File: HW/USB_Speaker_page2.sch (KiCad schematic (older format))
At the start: 3 parts

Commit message: Amplifier circuit using TPA6211A1-Q1
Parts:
- removed U?: OPA1678, symbol OPA1678
- added C14, C16: 10uF, symbol C_Small
- added C15, C17: 0.1uF, symbol C_Small
- added C? (x2): 0.22uF, symbol C_Small
- added U2, U3: TPA6211A1-Q1, symbol TPA6211A1-Q1
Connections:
- net labels added: GND, VBUS
- wire segments 0 -> 42
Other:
- moved on the sheet: LS1, LS2

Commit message: Switching out 2x TPA6211A1 for 1x TPA3137D2
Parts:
- added C? (x2): 1nF, symbol C_Small
- added C? (x2): 100nF, symbol C_Small
- added C? (x2): 10uF, symbol CP1_Small
- added C? (x2): 1uF, symbol C_Small
- added R? (x3): 10K, symbol R
- added U?: TPA3137D2, symbol TPA3137D2
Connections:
- wire segments 42 -> 98
- no-connect marks 0 -> 3
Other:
- note added: "PVCCL"
- note added: "PVCCR"

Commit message: Finsihed drawing amp circuit. Adding options and values later
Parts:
- removed C14, C16: 10uF, symbol C_Small
- removed C15, C17: 0.1uF, symbol C_Small
- removed C? (x2): 0.22uF, symbol C_Small
- removed R? (x2): 10K, symbol R
- removed U2, U3: TPA6211A1-Q1, symbol TPA6211A1-Q1
- added C? (x8): 1uF, symbol C_Small
- added C? (x4): 0.22uF, symbol C_Small
- added L? (x4): ?, symbol Ferrite_Bead_Small
- added R?: 10, symbol R
- added R?: NP, symbol R
- added R?: 0.0, symbol R
- added R? (x2): ?, symbol R
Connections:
- net labels added: PBTL, PLIMIT, Vin_L, Vin_R
- wire segments 98 -> 100
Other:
- note removed: "PVCCL"
- note removed: "PVCCR"
- moved on the sheet: C?, LS1, LS2, R?, U?

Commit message: ferrite chosen
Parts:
- L? (x4): value ? -> 300Ω@100MHz
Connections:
- net at R?.2, U?.1 (SDn): no longer U?.2 (FAULTn)
- new net FAULT: U?.2 (FAULTn)
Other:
- note added: "AND Gate \nhere"
- note added: "Use NFZ2MSM as output filter ferrite bead"
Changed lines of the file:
@@
 Connection ~ 5200 2700
 Wire Wire Line
-	3400 2050 3400 2500
-Wire Wire Line
 	3400 1750 3400 1650
 Wire Wire Line
-	3400 2300 3600 2300
-Wire Wire Line
-	3400 2500 3600 2500
+	2700 2300 3600 2300
+Wire Wire Line
+	3300 2500 3600 2500
 Connection ~ 3400 2300
 Wire Wire Line
@@
 Wire Wire Line
 	6200 3200 6200 3100
-Wire Wire Line
-	5800 3100 6400 3100
 Wire Wire Line
 	6400 3100 6400 3400
@@
 P 5700 3800
 F 0 "L?" V 5650 3700 50  0000 L CNN
-F 1 "?" V 5650 3900 50  0000 L CNN
+F 1 "300Ω@100MHz" V 5800 3650 50  0000 L CNN
 F 2 "" V 5630 3800 50  0001 C CNN
 F 3 "" H 5700 3800 50  0001 C CNN
@@
 P 5700 3100
 F 0 "L?" V 5650 3000 50  0000 L CNN
-F 1 "?" V 5650 3200 50  0000 L CNN
+F 1 "300Ω@100MHz" V 5800 2950 50  0000 L CNN
 F 2 "" V 5630 3100 50  0001 C CNN
 F 3 "" H 5700 3100 50  0001 C CNN
@@
 $EndComp
 Connection ~ 5150 3100
-Wire Wire Line
-	6000 3100 6000 3100
 Connection ~ 6200 3100
 Connection ~ 5150 3800
@@
 P 5700 4800
 F 0 "L?" V 5650 4700 50  0000 L CNN
-F 1 "?" V 5650 4900 50  0000 L CNN
+F 1 "300Ω@100MHz" V 5850 4650 50  0000 L CNN
 F 2 "" V 5630 4800 50  0001 C CNN
 F 3 "" H 5700 4800 50  0001 C CNN
@@
 P 5700 4100
 F 0 "L?" V 5650 4000 50  0000 L CNN
-F 1 "?" V 5650 4200 50  0000 L CNN
+F 1 "300Ω@100MHz" V 5800 3950 50  0000 L CNN
 F 2 "" V 5630 4100 50  0001 C CNN
 F 3 "" H 5700 4100 50  0001 C CNN
@@
 	3600 4500 2900 4500
 Connection ~ 2900 4500
+Text HLabel 1550 1900 0    60   Input ~ 0
+SSPNDn
+Wire Wire Line
+	3400 2050 3400 2300
+Text Label 3300 2500 0    60   ~ 0
+FAULT
+Text Label 1200 2100 0    60   ~ 0
+FAULT
+Wire Wire Line
+	1550 1900 1750 1900
+Wire Wire Line
+	1200 2100 1750 2100
+Wire Notes Line
+	1750 2200 1750 1750
+Wire Notes Line
+	1750 1750 2300 1750
+Wire Notes Line
+	2300 1750 2300 2200
+Wire Notes Line
+	2300 2200 1750 2200
+Wire Wire Line
+	2300 2000 2700 2000
+Wire Wire Line
+	2700 2000 2700 2300
+Text Notes 1850 2050 0    60   ~ 0
+AND Gate \nhere
+Wire Wire Line
+	5800 3100 6400 3100
+Text Notes 5600 2950 0    60   ~ 0
+Use NFZ2MSM as output filter ferrite bead
 $EndSCHEMATC

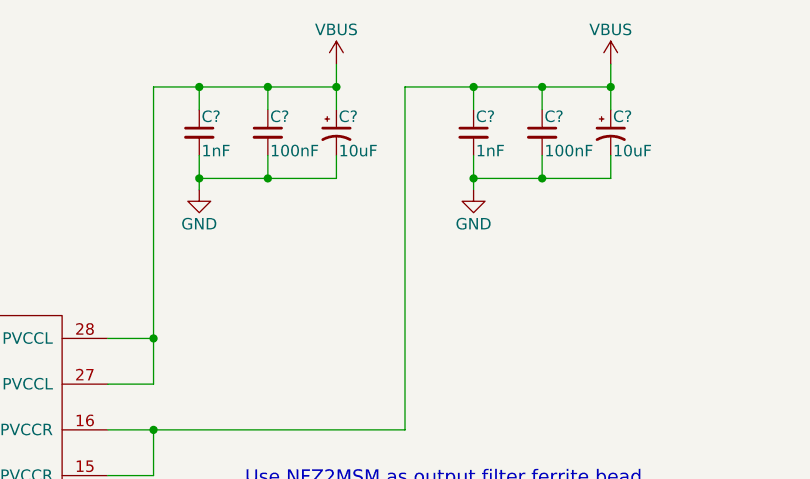
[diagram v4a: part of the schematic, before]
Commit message: Basic battery power supply topology
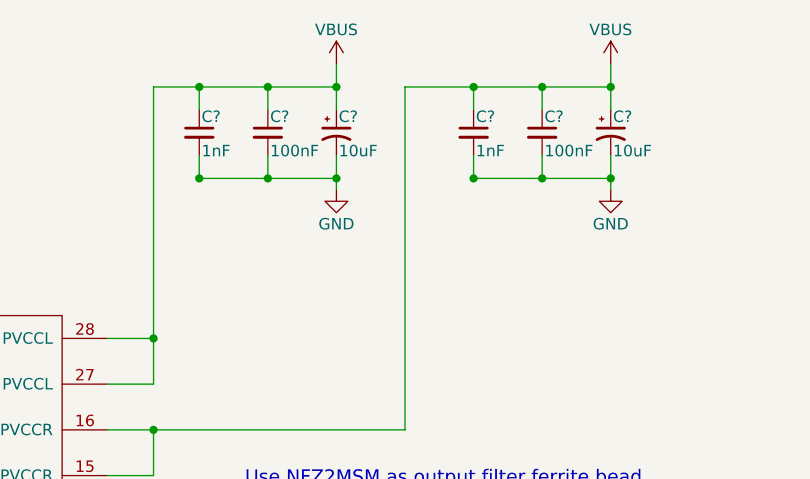
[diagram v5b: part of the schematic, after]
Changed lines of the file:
@@
 $Descr A4 11693 8268
 encoding utf-8
-Sheet 2 2
+Sheet 2 3
 Title ""
 Date ""
@@
 $EndComp
 $Comp
-L GND #PWR?
-U 1 1 5B29E616
-P 5400 1650
-F 0 "#PWR?" H 5400 1400 50  0001 C CNN
-F 1 "GND" H 5400 1500 50  0000 C CNN
-F 2 "" H 5400 1650 50  0001 C CNN
-F 3 "" H 5400 1650 50  0001 C CNN
-	1    5400 1650
-	1    0    0    -1
-$EndComp
-$Comp
 L C_Small C?
 U 1 1 5B2A1B92
@@
 L GND #PWR?
 U 1 1 5B2A1BAA
-P 6600 1650
-F 0 "#PWR?" H 6600 1400 50  0001 C CNN
-F 1 "GND" H 6600 1500 50  0000 C CNN
-F 2 "" H 6600 1650 50  0001 C CNN
-F 3 "" H 6600 1650 50  0001 C CNN
-	1    6600 1650
+P 7200 1650
+F 0 "#PWR?" H 7200 1400 50  0001 C CNN
+F 1 "GND" H 7200 1500 50  0000 C CNN
+F 2 "" H 7200 1650 50  0001 C CNN
+F 3 "" H 7200 1650 50  0001 C CNN
+	1    7200 1650
 	1    0    0    -1
 $EndComp
@@
 	6000 1100 6000 1300
 Wire Wire Line
-	5400 1500 5400 1650
+	5400 1500 5400 1600
 Connection ~ 6000 1200
 Wire Wire Line
@@
 	5400 1600 6000 1600
 Wire Wire Line
-	6000 1600 6000 1500
+	6000 1500 6000 1650
 Connection ~ 5700 1600
 Connection ~ 5400 1600
@@
 	6300 1200 7200 1200
 Wire Wire Line
-	6600 1500 6600 1650
+	6600 1500 6600 1600
 Connection ~ 7200 1200
 Wire Wire Line
@@
 	6600 1600 7200 1600
 Wire Wire Line
-	7200 1600 7200 1500
+	7200 1500 7200 1650
 Connection ~ 6900 1600
 Connection ~ 6600 1600
@@
 Text Notes 5600 2950 0    60   ~ 0
 Use NFZ2MSM as output filter ferrite bead
+$Comp
+L GND #PWR?
+U 1 1 5B29E616
+P 6000 1650
+F 0 "#PWR?" H 6000 1400 50  0001 C CNN
+F 1 "GND" H 6000 1500 50  0000 C CNN
+F 2 "" H 6000 1650 50  0001 C CNN
+F 3 "" H 6000 1650 50  0001 C CNN
+	1    6000 1650
+	1    0    0    -1
+$EndComp
+Connection ~ 6000 1600
+Connection ~ 7200 1600
 $EndSCHEMATC

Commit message: What did I do?
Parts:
- added C?: 1uF, symbol C_Small
- added U?: BU4S81G2, symbol BU4S81G2
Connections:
- net GND: now also C?.2, U?.3 (GND)
- net SSPNDn: now also U?.1 (A)
- net at R?.2, U?.1 (SDn): now also U?.4 (Y)
- net FAULT renamed FAULTn
- net FAULTn: now also U?.2 (B)
- net VBUS renamed +BATT
- net +BATT: now also C?.1, U?.5 (VCC)
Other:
- note added: "If SSDPNDn or FAULTn are active (LOW), shutdown ampifier"
- note removed: "AND Gate \nhere"
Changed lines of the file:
@@
-$EndComp
-$Comp
-L VBUS #PWR?
-U 1 1 5B29E207
-P 6000 1100
-F 0 "#PWR?" H 6000 950 50  0001 C CNN
-F 1 "VBUS" H 6000 1250 50  0000 C CNN
-F 2 "" H 6000 1100 50  0001 C CNN
-F 3 "" H 6000 1100 50  0001 C CNN
-	1    6000 1100
-	1    0    0    -1
 $EndComp
 $Comp
@@
 $EndComp
 $Comp
-L VBUS #PWR?
-U 1 1 5B2A1BA4
-P 7200 1100
-F 0 "#PWR?" H 7200 950 50  0001 C CNN
-F 1 "VBUS" H 7200 1250 50  0000 C CNN
-F 2 "" H 7200 1100 50  0001 C CNN
-F 3 "" H 7200 1100 50  0001 C CNN
-	1    7200 1100
-	1    0    0    -1
-$EndComp
-$Comp
 L GND #PWR?
 U 1 1 5B2A1BAA
@@
 F 3 "" H 7200 1650 50  0001 C CNN
 	1    7200 1650
-	1    0    0    -1
-$EndComp
-$Comp
-L VBUS #PWR?
-U 1 1 5B2A2F62
-P 3400 1650
-F 0 "#PWR?" H 3400 1500 50  0001 C CNN
-F 1 "VBUS" H 3400 1800 50  0000 C CNN
-F 2 "" H 3400 1650 50  0001 C CNN
-F 3 "" H 3400 1650 50  0001 C CNN
-	1    3400 1650
 	1    0    0    -1
 $EndComp
@@
 $EndComp
 $Comp
-L VBUS #PWR?
-U 1 1 5B2B0A32
-P 1450 3650
-F 0 "#PWR?" H 1450 3500 50  0001 C CNN
-F 1 "VBUS" H 1450 3800 50  0000 C CNN
-F 2 "" H 1450 3650 50  0001 C CNN
-F 3 "" H 1450 3650 50  0001 C CNN
-	1    1450 3650
-	1    0    0    -1
-$EndComp
-$Comp
 L R R?
 U 1 1 5B2B163A
@@
 $EndComp
 $Comp
-L VBUS #PWR?
-U 1 1 5B2B27B1
-P 2900 4000
-F 0 "#PWR?" H 2900 3850 50  0001 C CNN
-F 1 "VBUS" H 2900 4150 50  0000 C CNN
-F 2 "" H 2900 4000 50  0001 C CNN
-F 3 "" H 2900 4000 50  0001 C CNN
-	1    2900 4000
-	1    0    0    -1
-$EndComp
-$Comp
 L TPA3137D2 U?
 U 1 1 5B29D076
 P 3800 5400
-F 0 "U?" H 3850 8550 60  0000 C CNN
+F 0 "U?" H 3850 8650 60  0000 C CNN
 F 1 "TPA3137D2" H 4050 5450 60  0000 C CNN
 F 2 "" H 3800 5550 60  0001 C CNN
@@
 $EndComp
 $Comp
-L VBUS #PWR?
-U 1 1 5B2B5C0D
-P 1200 3650
-F 0 "#PWR?" H 1200 3500 50  0001 C CNN
-F 1 "VBUS" H 1200 3800 50  0000 C CNN
-F 2 "" H 1200 3650 50  0001 C CNN
-F 3 "" H 1200 3650 50  0001 C CNN
-	1    1200 3650
-	1    0    0    -1
-$EndComp
-$Comp
 L GND #PWR?
 U 1 1 5B2B5C69
@@
 Connection ~ 5200 2700
 Wire Wire Line
-	3400 1750 3400 1650
+	3400 1650 3400 1750
 Wire Wire Line
 	2700 2300 3600 2300
@@
 	3500 4900 3600 4900
 Wire Wire Line
-	2900 4050 2900 4000
-Wire Wire Line
-	1450 3650 1450 3700
+	2900 3950 2900 4050
+Wire Wire Line
+	1450 3600 1450 3700
 Wire Wire Line
 	1450 4700 1450 4600
@@
 	1200 4700 1200 4600
 Wire Wire Line
-	1200 3700 1200 3650
+	1200 3600 1200 3700
 Wire Wire Line
 	3200 2700 3600 2700
@@
 	3600 4500 2900 4500
 Connection ~ 2900 4500
-Text HLabel 1550 1900 0    60   Input ~ 0
+Text HLabel 1100 1850 0    60   Input ~ 0
 SSPNDn
 Wire Wire Line
 	3400 2050 3400 2300
 Text Label 3300 2500 0    60   ~ 0
-FAULT
-Text Label 1200 2100 0    60   ~ 0
-FAULT
-Wire Wire Line
-	1550 1900 1750 1900
-Wire Wire Line
-	1200 2100 1750 2100
-Wire Notes Line
-	1750 2200 1750 1750
-Wire Notes Line
-	1750 1750 2300 1750
-Wire Notes Line
-	2300 1750 2300 2200
-Wire Notes Line
-	2300 2200 1750 2200
-Wire Wire Line
-	2300 2000 2700 2000
-Wire Wire Line
-	2700 2000 2700 2300
-Text Notes 1850 2050 0    60   ~ 0
-AND Gate \nhere
+FAULTn
+Text Label 750  2150 0    60   ~ 0
+FAULTn
+Wire Wire Line
+	1100 1850 1300 1850
+Wire Wire Line
+	750  2150 1300 2150
 Wire Wire Line
 	5800 3100 6400 3100
@@
 Connection ~ 6000 1600
 Connection ~ 7200 1600
+$Comp
+L GND #PWR?
+U 1 1 5B34535C
+P 1750 2550
+F 0 "#PWR?" H 1750 2300 50  0001 C CNN
+F 1 "GND" H 1750 2400 50  0000 C CNN
+F 2 "" H 1750 2550 50  0001 C CNN
+F 3 "" H 1750 2550 50  0001 C CNN
+	1    1750 2550
+	1    0    0    -1
+$EndComp
+Wire Wire Line
+	1750 2550 1750 2450
+Wire Wire Line
+	1750 1100 1750 1550
+Text Notes 650  800  0    60   ~ 0
+If SSDPNDn or FAULTn are active (LOW), shutdown ampifier
+$Comp
+L +BATT #PWR?
+U 1 1 5B34843E
+P 1200 3600
+F 0 "#PWR?" H 1200 3450 50  0001 C CNN
+F 1 "+BATT" H 1200 3740 50  0000 C CNN
+F 2 "" H 1200 3600 50  0001 C CNN
+F 3 "" H 1200 3600 50  0001 C CNN
+	1    1200 3600
+	1    0    0    -1
+$EndComp
+$Comp
+L +BATT #PWR?
+U 1 1 5B3484B6
+P 1450 3600
+F 0 "#PWR?" H 1450 3450 50  0001 C CNN
+F 1 "+BATT" H 1450 3740 50  0000 C CNN
+F 2 "" H 1450 3600 50  0001 C CNN
+F 3 "" H 1450 3600 50  0001 C CNN
+	1    1450 3600
+	1    0    0    -1
+$EndComp
+$Comp
+L +BATT #PWR?
+U 1 1 5B348527
+P 3400 1650
+F 0 "#PWR?" H 3400 1500 50  0001 C CNN
+F 1 "+BATT" H 3400 1790 50  0000 C CNN
+F 2 "" H 3400 1650 50  0001 C CNN
+F 3 "" H 3400 1650 50  0001 C CNN
+	1    3400 1650
+	1    0    0    -1
+$EndComp
+$Comp
+L +BATT #PWR?
+U 1 1 5B348598
+P 6000 1100
+F 0 "#PWR?" H 6000 950 50  0001 C CNN
+F 1 "+BATT" H 6000 1240 50  0000 C CNN
+F 2 "" H 6000 1100 50  0001 C CNN
+F 3 "" H 6000 1100 50  0001 C CNN
+	1    6000 1100
+	1    0    0    -1
+$EndComp
+$Comp
+L +BATT #PWR?
+U 1 1 5B348609
+P 7200 1100
+F 0 "#PWR?" H 7200 950 50  0001 C CNN
+F 1 "+BATT" H 7200 1240 50  0000 C CNN
+F 2 "" H 7200 1100 50  0001 C CNN
+F 3 "" H 7200 1100 50  0001 C CNN
+	1    7200 1100
+	1    0    0    -1
+$EndComp
+$Comp
+L +BATT #PWR?
+U 1 1 5B3486E0
+P 2900 3950
+F 0 "#PWR?" H 2900 3800 50  0001 C CNN
+F 1 "+BATT" H 2900 4090 50  0000 C CNN
+F 2 "" H 2900 3950 50  0001 C CNN
+F 3 "" H 2900 3950 50  0001 C CNN
+	1    2900 3950
+	1    0    0    -1
+$EndComp
+$Comp
+L BU4S81G2 U?
+U 1 1 5B34B097
+P 1500 2750
+F 0 "U?" H 1850 3900 60  0000 C CNN
+F 1 "BU4S81G2" H 2000 3800 60  0000 C CNN
+F 2 "" H 1500 2750 60  0001 C CNN
+F 3 "" H 1500 2750 60  0001 C CNN
+	1    1500 2750
+	1    0    0    -1
+$EndComp
+$Comp
+L +BATT #PWR?
+U 1 1 5B34B179
+P 1750 1100
+F 0 "#PWR?" H 1750 950 50  0001 C CNN
+F 1 "+BATT" H 1750 1240 50  0000 C CNN
+F 2 "" H 1750 1100 50  0001 C CNN
+F 3 "" H 1750 1100 50  0001 C CNN
+	1    1750 1100
+	1    0    0    -1
+$EndComp
+$Comp
+L C_Small C?
+U 1 1 5B34BCCE
+P 1400 1350
+F 0 "C?" H 1410 1420 50  0000 L CNN
+F 1 "1uF" H 1410 1270 50  0000 L CNN
+F 2 "" H 1400 1350 50  0001 C CNN
+F 3 "" H 1400 1350 50  0001 C CNN
+	1    1400 1350
+	1    0    0    -1
+$EndComp
+Wire Wire Line
+	1400 1250 1400 1150
+Wire Wire Line
+	1400 1150 1750 1150
+Connection ~ 1750 1150
+$Comp
+L GND #PWR?
+U 1 1 5B34CF56
+P 1400 1500
+F 0 "#PWR?" H 1400 1250 50  0001 C CNN
+F 1 "GND" H 1400 1350 50  0000 C CNN
+F 2 "" H 1400 1500 50  0001 C CNN
+F 3 "" H 1400 1500 50  0001 C CNN
+	1    1400 1500
+	1    0    0    -1
+$EndComp
+Wire Wire Line
+	1400 1500 1400 1450
+Wire Wire Line
+	2700 2300 2700 2000
+Wire Wire Line
+	2700 2000 2300 2000
 $EndSCHEMATC

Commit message: Added LEDs, Test points, and ESD protection on USB
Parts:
- added J? (x3): TP, symbol TEST_1P
- LS1, LS2: value Speaker -> 2W Speaker
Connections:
- net PBTL: now also J?.1
- net PLIMIT: now also J?.1
- net at R?.2, U?.1 (SDn), U?.4 (Y): now also J?.1

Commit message: First draft done :100:
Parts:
- R19: renamed from R?; value ? -> 0.0
- R22: renamed from R?; value ? -> NP
- gave numbers to parts that had none: 34
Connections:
- net +BATT: no longer R19.1
- net GVDD: now reaches C34.1, U3.9 (GVDD)
- net GVDD: now also R19.1
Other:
- note added: "Power consumption limit??\n"
